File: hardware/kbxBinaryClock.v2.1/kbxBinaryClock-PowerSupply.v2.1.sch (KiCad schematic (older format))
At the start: 8 parts, among them J1 Jack-DC, U5 LD1117S33TR

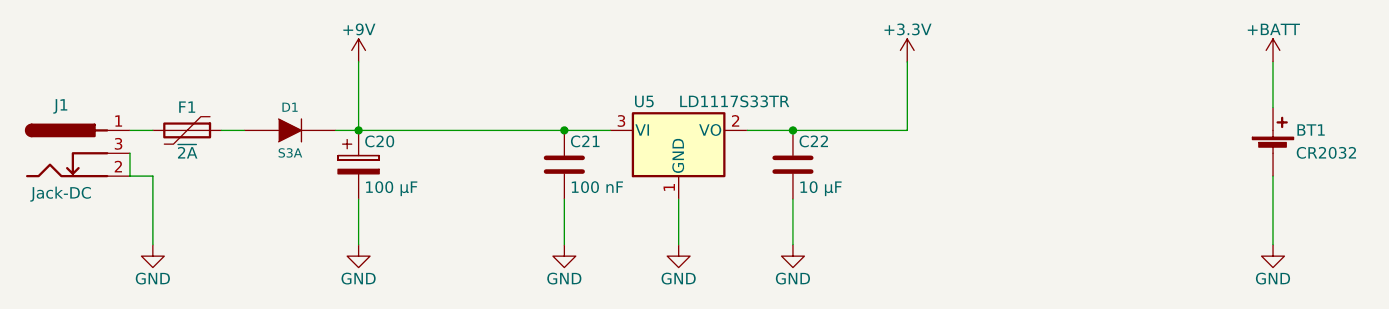
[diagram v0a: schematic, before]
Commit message: Added BoM, hw README, PCB tweaks
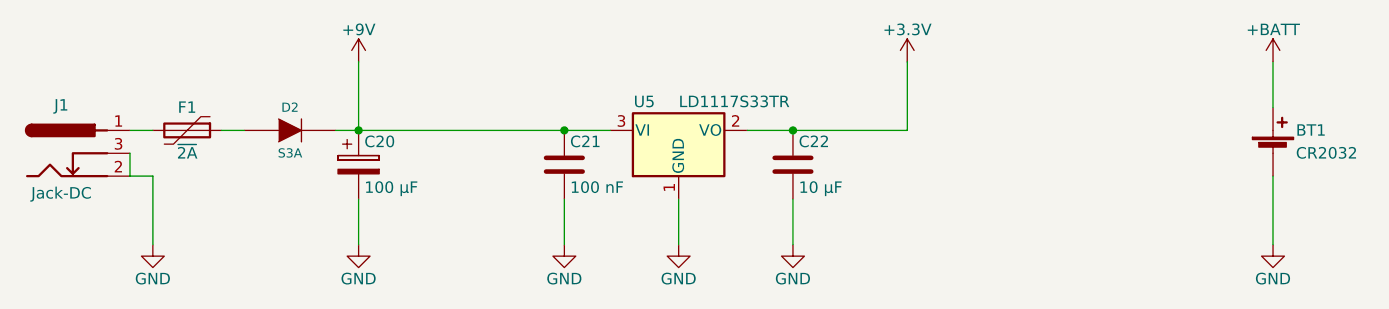
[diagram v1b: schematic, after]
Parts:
- renumbered D1 to D2
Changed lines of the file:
@@
 $EndComp
 $Comp
-L DIODE D1
+L DIODE D2
 U 1 1 5A0B6C19
 P 3900 3900
-F 0 "D1" H 3900 4000 40  0000 C CNN
+F 0 "D2" H 3900 4000 40  0000 C CNN
 F 1 "S3A" H 3900 3800 40  0000 C CNN
 F 2 "Diodes_SMD:D_SMC" H 3900 3900 60  0001 C CNN

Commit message: Updated for KiCad v5, updated silks
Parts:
- BT1: symbol Battery_Cell -> Device:Battery_Cell
- C20: symbol CP -> Device:CP
- C21, C22: symbol C -> Device:C
- D2: symbol DIODE -> win:DIODE
- F1: symbol Polyfuse -> Device:Polyfuse
- J1: symbol Jack-DC -> kbxBinaryClock.v2.1-rescue:Jack-DC
- U5: symbol LD1117S33TR_SOT223 -> win:LD1117S33TR_SOT223
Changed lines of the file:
@@
-EESchema Schematic File Version 2
-LIBS:power
-LIBS:device
-LIBS:transistors
-LIBS:conn
-LIBS:linear
-LIBS:regul
-LIBS:74xx
-LIBS:cmos4000
-LIBS:adc-dac
-LIBS:memory
-LIBS:xilinx
-LIBS:microcontrollers
-LIBS:dsp
-LIBS:microchip
-LIBS:analog_switches
-LIBS:motorola
-LIBS:texas
-LIBS:intel
-LIBS:audio
-LIBS:interface
-LIBS:digital-audio
-LIBS:philips
-LIBS:display
-LIBS:cypress
-LIBS:siliconi
-LIBS:opto
-LIBS:atmel
-LIBS:contrib
-LIBS:valves
-LIBS:stm32
-LIBS:win
-LIBS:mechanical
-LIBS:switches
-LIBS:maxim
-LIBS:sensors
+EESchema Schematic File Version 4
 LIBS:kbxBinaryClock.v2.1-cache
-EELAYER 25 0
+EELAYER 26 0
 EELAYER END
 $Descr A4 11693 8268
@@
 $EndDescr
 $Comp
-L Jack-DC J1
+L kbxBinaryClock.v2.1-rescue:Jack-DC J1
 U 1 1 5A06C211
 P 2900 4000
@@
 $EndComp
 $Comp
-L C C22
+L Device:C C22
 U 1 1 5A06C24E
 P 6100 4050
@@
 $EndComp
 $Comp
-L C C21
+L Device:C C21
 U 1 1 5A06C283
 P 5100 4050
@@
 $EndComp
 $Comp
-L Battery_Cell BT1
+L Device:Battery_Cell BT1
 U 1 1 5A06C2CC
 P 8200 4000
@@
 $EndComp
 $Comp
-L CP C20
+L Device:CP C20
 U 1 1 5A0AB81C
 P 4200 4050
@@
 $EndComp
 $Comp
-L +BATT #PWR027
+L power:+BATT #PWR027
 U 1 1 5A0AB8E2
 P 8200 3600
@@
 $EndComp
 $Comp
-L +3.3V #PWR028
+L power:+3.3V #PWR028
 U 1 1 5A0AB93A
 P 6600 3600
@@
 $EndComp
 $Comp
-L GND #PWR029
+L power:GND #PWR029
 U 1 1 5A0ABA04
 P 4200 4400
@@
 $EndComp
 $Comp
-L GND #PWR030
+L power:GND #PWR030
 U 1 1 5A0ABA30
 P 5100 4400
@@
 $EndComp
 $Comp
-L GND #PWR031
+L power:GND #PWR031
 U 1 1 5A0ABA5C
 P 5600 4400
@@
 $EndComp
 $Comp
-L GND #PWR032
+L power:GND #PWR032
 U 1 1 5A0ABA88
 P 6100 4400
@@
 $EndComp
 $Comp
-L GND #PWR033
+L power:GND #PWR033
 U 1 1 5A0ABAB4
 P 8200 4400
@@
 $EndComp
 $Comp
-L +9V #PWR034
+L power:+9V #PWR034
 U 1 1 5A0AC145
 P 4200 3600
@@
 $EndComp
 $Comp
-L Polyfuse F1
+L Device:Polyfuse F1
 U 1 1 5A0B6BAC
 P 3450 3900
@@
 $EndComp
 $Comp
-L DIODE D2
+L win:DIODE D2
 U 1 1 5A0B6C19
 P 3900 3900
@@
 $EndComp
 $Comp
-L GND #PWR035
+L power:GND #PWR035
 U 1 1 5A0B6F52
 P 3300 4400
@@
 $EndComp
 $Comp
-L LD1117S33TR_SOT223 U5
+L win:LD1117S33TR_SOT223 U5
 U 1 1 5A06C0AF
 P 5600 3900
